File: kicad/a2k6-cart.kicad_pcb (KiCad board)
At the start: 2 copper layers, 41.7 x 47.8 mm, 4 parts, among them J1 2600_Cartridge_Port, U1 2732, U2 74LS04

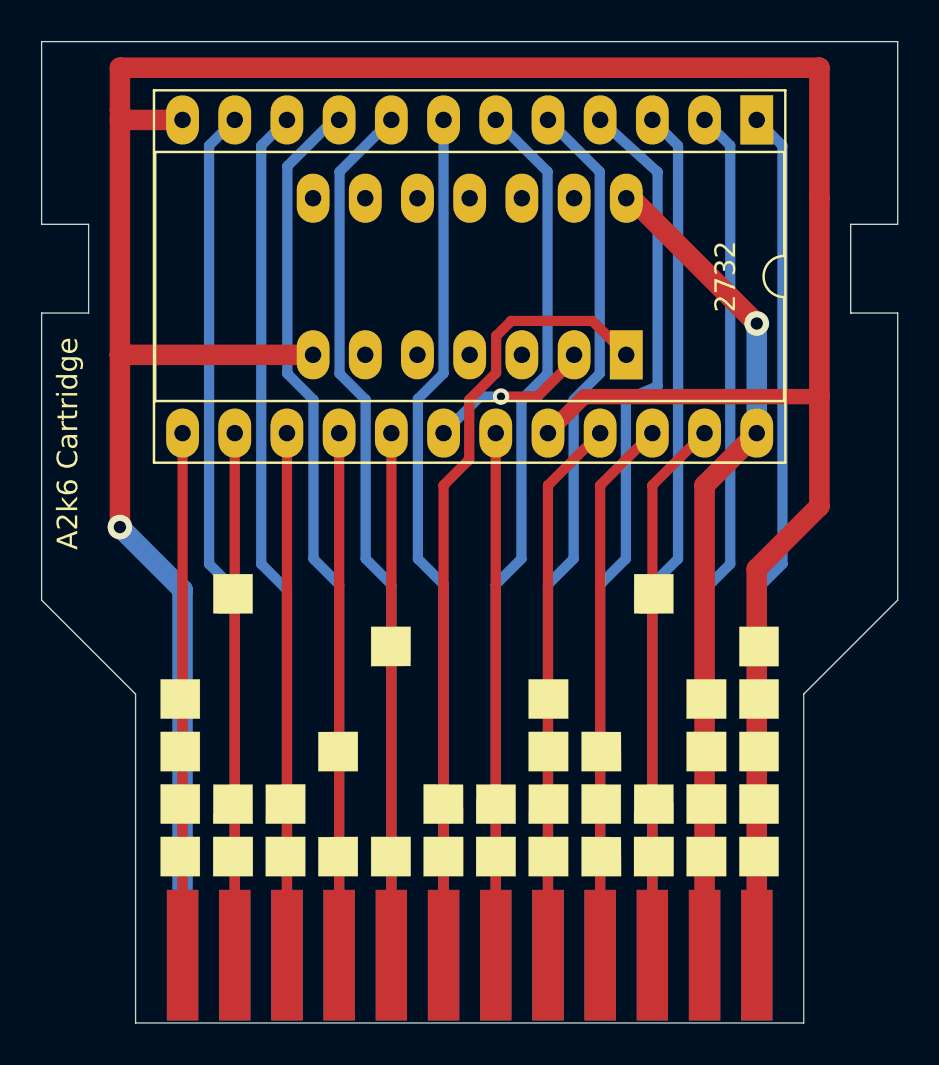
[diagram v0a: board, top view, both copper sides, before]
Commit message: take off 0.4 mm from the sides of the pcb
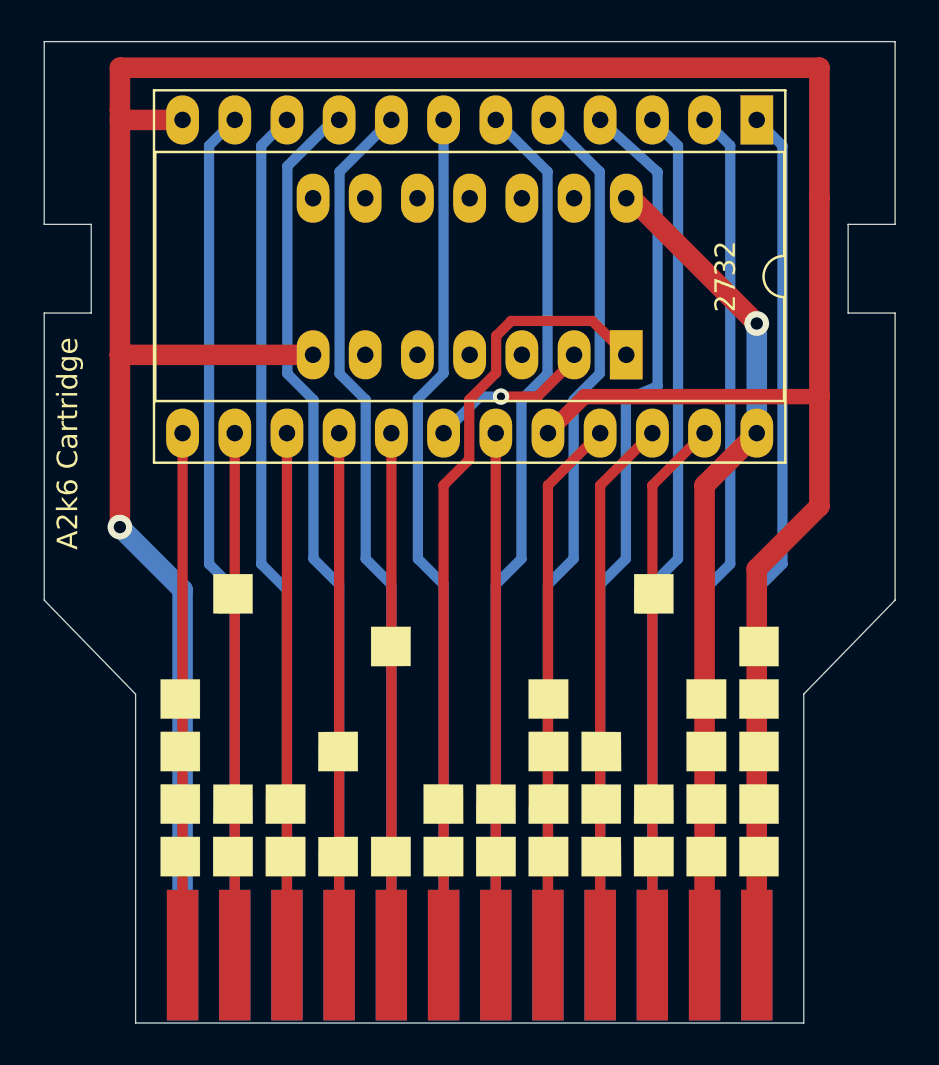
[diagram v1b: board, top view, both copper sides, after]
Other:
- board size 41.7 x 47.8 mm -> 41.4 x 47.8 mm
